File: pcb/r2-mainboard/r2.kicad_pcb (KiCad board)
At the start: 4 copper layers, 85.5 x 82.8 mm, 328 parts, among them J20 SWD+JTAG (DNP), J200 USB-C 16P, J201 Pico-Lock 504050-0391, J202 SolderPads 3x, J21 MICRO_SD(TFC-WPAPR-08), J22 HC-FPC-05-09-6RLTAG, J24 HC-FPC-05-09-8RLTAG, J26 BTH-060-01-L-D-A-K-TR, J27 BTH-060-01-L-D-A-K-TR, J28 USB-C 16P, J6 XF2M-4015-1A, Q1 AO3401A, Q2 S8050, Q6 AO3400A, Q7 AO3401A, Q8 AO3401A, Q9 AO3400A, SW20 EVQPUC02K, SW21 SW, SW22 SW, U20 STM32G0B1RCT6, U200 BQ25892RTW, U201 MAX17048G+T10, U21 INA3221, U22 INA3221, U23 LGS6302B5, U24 LGS6302B5, U26 LGS5145, U27 INA3221, U3 USBLC6-2SC6, U300 TPS7A0233DBVR, U301 TPS61022RWUR, U302 TPS63802DLAR, U303 TPS62A02DRLR, U304 TPS62A02DRLR, U31 LM321, U41 XC6SLX-FTG256, U52 MT41K64M16TW, U53 LM3630A, U54 TPS22914BYFPR, U56 TPS2553DBVR, U57 USBLC6-2SC6, U6 MT9700, U7 TPS22914BYFPR, U8 TPS22914BYFPR, U9 LGS5145, U902 W25Q128JVSIQ, X1 33.33MHz, X2 PCM-071, Y20 32.768kHz

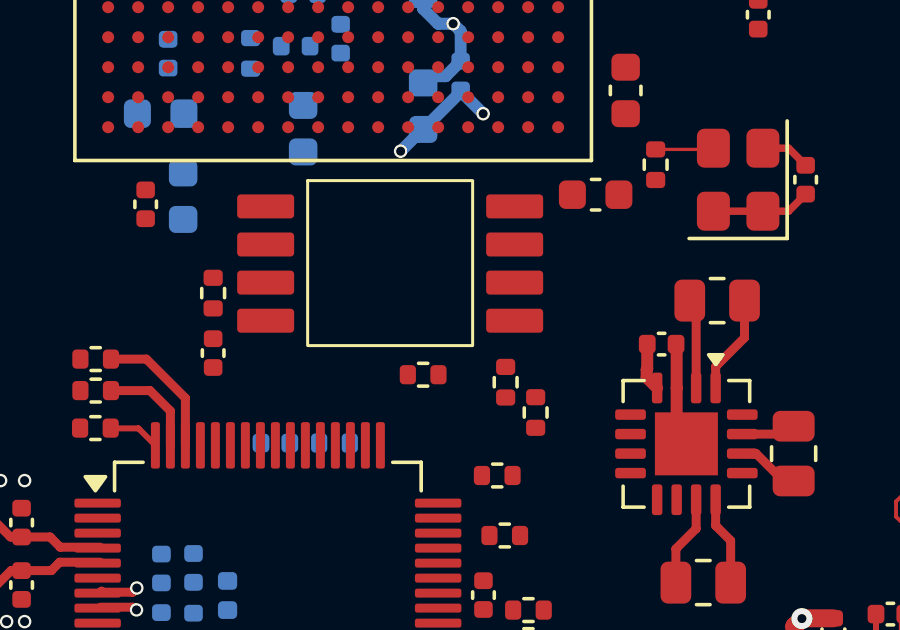
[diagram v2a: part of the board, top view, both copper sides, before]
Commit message: Declare the owner's Reflow symbol library; drop the dead library.pretty
U902 (the config NOR, was U42) uses lib_id "Reflow:WSON_Flash", but
sym-lib-table declared only "symbols" and "r2", so KiCad would report it
as a missing symbol and offer to rescue it. Declared:

  Reflow -> ${KIPRJMOD}/library/Reflow.kicad_sym

fp-lib-table also carried an entry for ${KIPRJMOD}/library.pretty, which
does not exist on disk -- an error on every project open. The real
footprint library is library/Reflow.pretty and was already declared
separately as "Reflow", so the dead entry is removed.

Verified: the netlist exports with no warnings and U902's eight nodes are
identical to what U42 had -- pin 1 NOR_CS#, 2 FPGA_MOSI, 3 NOR_IO2,
4 GND, 5 FPGA_MISO, 6 FPGA_SCLK, 7 NOR_IO3, 8 +3V3.

Not changed: tutorial_lib.kicad_sym (4 symbols) is still undeclared, and
r2.pretty is untouched -- its 8 footprints all remain in use.

Co-Authored-By: Claude Opus 5 <noreply@anthropic.com>
Claude-Session: https://claude.ai/code/session_01MHTAe6ZnhogTEgtyPcLhwG
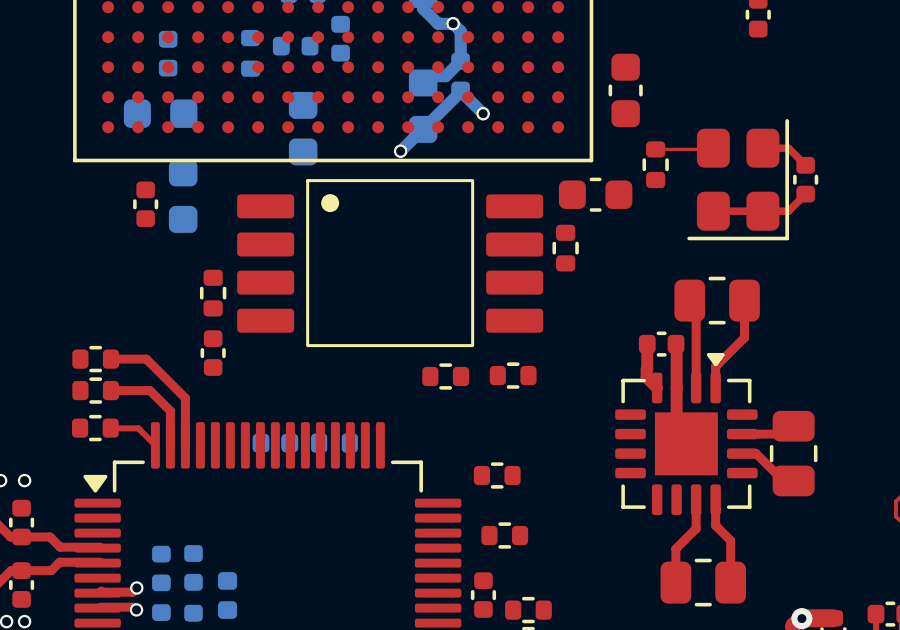
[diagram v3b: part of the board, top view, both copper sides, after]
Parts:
- moved R413 11.8 mm to (221.2, 91.2), turned to -90 degrees
- moved R412 7.51 mm to (209.5, 92.8), turned to 90 degrees
- moved R411 3.23 mm to (217.2, 95.5), turned to 180 degrees
- moved R410 0.33 mm to (219.5, 95.5), turned to 180 degrees
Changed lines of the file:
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@@
 	(footprint "Resistor_SMD:R_0402_1005Metric"
 		(layer "F.Cu")
-		(at 219.25 95.72 90)
+		(at 219.5 95.5 180)
 		(descr "Resistor SMD 0402 (1005 Metric), square (rectangular) end terminal, IPC-7351 nominal, (Body size source: IPC-SM-782 page 72, https://www.pcb-3d.com/wordpress/wp-content/uploads/ipc-sm-782a_amendment_1_and_2.pdf)")
 		(tags "resistor")
 		(property "Reference" "R410"
-			(at 0 -1.17 90)
+			(at 0 -1.17 0)
 			(layer "F.SilkS")
 			(hide yes)
@@
 		)
 		(property "Value" "10k"
-			(at 0 1.17 90)
+			(at 0 1.17 0)
 			(layer "F.Fab")
 			(effects
@@
 		)
 		(property "Datasheet" ""
-			(at 0 0 90)
+			(at 0 0 0)
 			(layer "F.Fab")
 			(hide yes)
@@
 		)
 		(property "Description" "NOR_CS# pull-up -- holds the flash deselected when neither the FPGA nor the SoM drives it"
-			(at 0 0 90)
+			(at 0 0 0)
 			(layer "F.Fab")
 			(hide yes)
@@
 		)
 		(property "KiLib_Generator" "SMD_2terminal_chip_molded"
-			(at 0 0 90)
+			(at 0 0 0)
 			(layer "F.SilkS")
 			(hide yes)
@@
 		(duplicate_pad_numbers_are_jumpers no)
 		(fp_line
-			(start -0.153641 -0.38)
-			(end 0.153641 -0.38)
+			(start -0.153641 0.38)
+			(end 0.153641 0.38)
 			(stroke
 				(width 0.12)
@@
 		)
 		(fp_line
-			(start -0.153641 0.38)
-			(end 0.153641 0.38)
+			(start -0.153641 -0.38)
+			(end 0.153641 -0.38)
 			(stroke
 				(width 0.12)
@@
 		)
 		(fp_text user "${REFERENCE}"
-			(at 0 0 90)
+			(at 0 0 180)
 			(unlocked yes)
 			(layer "F.Fab")
@@
 		)
 		(pad "1" smd roundrect
-			(at -0.51 0 90)
+			(at -0.51 0 180)
 			(size 0.54 0.64)
 			(layers "F.Cu" "F.Mask" "F.Paste")
@@
 		)
 		(pad "2" smd roundrect
-			(at 0.51 0 90)
+			(at 0.51 0 180)
 			(size 0.54 0.64)
 			(layers "F.Cu" "F.Mask" "F.Paste")
@@
 		(sheetname "/fpga_config/")
 		(sheetfile "fpga_config.kicad_sch")
-		(units
-			(unit
-				(name "A")
-				(pins "5" "2" "3" "7" "6" "1" "8" "4")
-			)
-		)
 		(attr smd)
 		(duplicate_pad_numbers_are_jumpers no)
@@
 			(layer "F.SilkS")
 		)
+		(fp_circle
+			(center -2 -2)
+			(end -2 -2.25)
+			(stroke
+				(width 0.1)
+				(type solid)
+			)
+			(fill yes)
+			(layer "F.SilkS")
+		)
 		(pad "1" smd roundrect
 			(at -4.15 -1.89)
@@
 		)
 		(pad "5" smd roundrect
-			(at 4.15 -1.89)
+			(at 4.15 1.92)
 			(size 1.9 0.8)
 			(layers "F.Cu" "F.Mask" "F.Paste")
@@
 		)
 		(pad "6" smd roundrect
-			(at 4.15 -0.62)
+			(at 4.15 0.65)
 			(size 1.9 0.8)
 			(layers "F.Cu" "F.Mask" "F.Paste")
@@
 		)
 		(pad "7" smd roundrect
-			(at 4.15 0.65)
+			(at 4.15 -0.62)
 			(size 1.9 0.8)
 			(layers "F.Cu" "F.Mask" "F.Paste")
@@
 		)
 		(pad "8" smd roundrect
-			(at 4.15 1.92)
+			(at 4.15 -1.89)
 			(size 1.9 0.8)
 			(layers "F.Cu" "F.Mask" "F.Paste")
@@
 	(footprint "Resistor_SMD:R_0402_1005Metric"
 		(layer "F.Cu")
-		(at 216.5 95.47)
+		(at 209.5 92.75 90)
 		(descr "Resistor SMD 0402 (1005 Metric), square (rectangular) end terminal, IPC-7351 nominal, (Body size source: IPC-SM-782 page 72, https://www.pcb-3d.com/wordpress/wp-content/uploads/ipc-sm-782a_amendment_1_and_2.pdf)")
 		(tags "resistor")
 		(property "Reference" "R412"
-			(at 0 -1.17 0)
+			(at 0 -1.17 90)
 			(layer "F.SilkS")
 			(hide yes)
@@
 		)
 		(property "Value" "10k"
-			(at 0 1.17 0)
+			(at 0 1.17 90)
 			(layer "F.Fab")
 			(effects
@@
 		)
 		(property "Datasheet" ""
-			(at 0 0 0)
+			(at 0 0 90)
 			(layer "F.Fab")
 			(hide yes)
@@
 		)
 		(property "Description" "UG380 Fig 2-13 note 4: MISO[2]/MISO[3] need pull-ups to VCCO_2."
-			(at 0 0 0)
+			(at 0 0 90)
 			(layer "F.Fab")
 			(hide yes)
@@
 		)
 		(property "KiLib_Generator" "SMD_2terminal_chip_molded"
-			(at 0 0 0)
+			(at 0 0 90)
 			(layer "F.SilkS")
 			(hide yes)
@@
 		)
 		(fp_text user "${REFERENCE}"
-			(at 0 0 0)
+			(at 0 0 90)
 			(unlocked yes)
 			(layer "F.Fab")
@@
 		)
 		(pad "1" smd roundrect
-			(at -0.51 0)
+			(at -0.51 0 90)
 			(size 0.54 0.64)
 			(layers "F.Cu" "F.Mask" "F.Paste")
@@
 		)
 		(pad "2" smd roundrect
-			(at 0.51 0)
+			(at 0.51 0 90)
 			(size 0.54 0.64)
 			(layers "F.Cu" "F.Mask" "F.Paste")
@@
 	(footprint "Resistor_SMD:R_0402_1005Metric"
 		(layer "F.Cu")
-		(at 209.5 92.75 90)
+		(at 221.25 91.25 -90)
 		(descr "Resistor SMD 0402 (1005 Metric), square (rectangular) end terminal, IPC-7351 nominal, (Body size source: IPC-SM-782 page 72, https://www.pcb-3d.com/wordpress/wp-content/uploads/ipc-sm-782a_amendment_1_and_2.pdf)")
 		(tags "resistor")
@@
 		(duplicate_pad_numbers_are_jumpers no)
 		(fp_line
-			(start -0.153641 -0.38)
-			(end 0.153641 -0.38)
+			(start -0.153641 0.38)
+			(end 0.153641 0.38)
 			(stroke
 				(width 0.12)
@@
 		)
 		(fp_line
-			(start -0.153641 0.38)
-			(end 0.153641 0.38)
+			(start -0.153641 -0.38)
+			(end 0.153641 -0.38)
 			(stroke
 				(width 0.12)
@@
 		)
 		(fp_text user "${REFERENCE}"
-			(at 0 0 90)
+			(at 0 0 270)
 			(unlocked yes)
 			(layer "F.Fab")
@@
 		)
 		(pad "1" smd roundrect
-			(at -0.51 0 90)
+			(at -0.51 0 270)
 			(size 0.54 0.64)
 			(layers "F.Cu" "F.Mask" "F.Paste")
@@
 		)
 		(pad "2" smd roundrect
-			(at 0.51 0 90)
+			(at 0.51 0 270)
 			(size 0.54 0.64)
 			(layers "F.Cu" "F.Mask" "F.Paste")
@@
 	(footprint "Resistor_SMD:R_0402_1005Metric"
 		(layer "F.Cu")
-		(at 220.25 96.73 90)
+		(at 217.25 95.53 180)
 		(descr "Resistor SMD 0402 (1005 Metric), square (rectangular) end terminal, IPC-7351 nominal, (Body size source: IPC-SM-782 page 72, https://www.pcb-3d.com/wordpress/wp-content/uploads/ipc-sm-782a_amendment_1_and_2.pdf)")
 		(tags "resistor")
 		(property "Reference" "R411"
-			(at 0 -1.17 90)
+			(at 0 -1.17 0)
 			(layer "F.SilkS")
 			(hide yes)
@@
 		)
 		(property "Value" "100R"
-			(at 0 1.17 90)
+			(at 0 1.17 0)
 			(layer "F.Fab")
 			(effects
@@
 		)
 		(property "Datasheet" ""
-			(at 0 0 90)
+			(at 0 0 0)
 			(layer "F.Fab")
 			(hide yes)
@@
 		)
 		(property "Description" "Series limit on the SoM's NOR chip select: the FPGA drives CSO_B during configuration, so the two briefly contend if software gets it wrong"
-			(at 0 0 90)
+			(at 0 0 0)
 			(layer "F.Fab")
 			(hide yes)
@@
 		)
 		(property "KiLib_Generator" "SMD_2terminal_chip_molded"
-			(at 0 0 90)
+			(at 0 0 0)
 			(layer "F.SilkS")
 			(hide yes)
@@
 		(duplicate_pad_numbers_are_jumpers no)
 		(fp_line
-			(start -0.153641 -0.38)
-			(end 0.153641 -0.38)
+			(start -0.153641 0.38)
+			(end 0.153641 0.38)
 			(stroke
 				(width 0.12)
@@
 		)
 		(fp_line
-			(start -0.153641 0.38)
-			(end 0.153641 0.38)
+			(start -0.153641 -0.38)
+			(end 0.153641 -0.38)
 			(stroke
 				(width 0.12)
@@
 		)
 		(fp_text user "${REFERENCE}"
-			(at 0 0 90)
+			(at 0 0 180)
 			(unlocked yes)
 			(layer "F.Fab")
@@
 		)
 		(pad "1" smd roundrect
-			(at -0.51 0 90)
+			(at -0.51 0 180)
 			(size 0.54 0.64)
 			(layers "F.Cu" "F.Mask" "F.Paste")
@@
 		)
 		(pad "2" smd roundrect
-			(at 0.51 0 90)
+			(at 0.51 0 180)
 			(size 0.54 0.64)
 			(layers "F.Cu" "F.Mask" "F.Paste")

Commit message: Recover from the KiCad crash; finish the USB1_D+/D- rename
KiCad crashed and deleted 150 tracked files plus 19 untracked ones.
Recovery, in the order that matters:

  1. copied _restore_backup_2026-08-31T20-57-08-688 aside (261 MB)
  2. rescued the 4 untracked files that existed only there -- the
     PHYTEC PCM-071 STEP/x_t/Basic models and the library/3dmodels copy.
     The other 15 were __pycache__, .lck and .bak.
  3. git checkout of the 150 deletions (deletions only, so the six
     modified files were never touched)
  4. three files the crash had *rolled back* rather than deleted, and
     which git checkout therefore missed, restored from HEAD:
       r2.kicad_sym    -- was 11 symbols, missing TPS2553DBV,
                          BTH-060_AB/CD and BOM_ITEM, and carrying the
                          superseded PCM-071 symbol: the pre-2026-08-20
                          state, before the SoM was split in two
       sym-lib-table   -- had lost the Reflow declaration
       fp-lib-table    -- had lost Reflow and (version 7)

r2.kicad_pcb was not damaged -- 328 footprints, 471 segments, same as
HEAD. Rescuing PCM-071_1573-1.STEP also repairs X2's 3D model path,
which an earlier restore had broken.

Separately, the USB1 net rename is finished at the owner's request:
som.kicad_sch USB1_DM/DP -> USB1_D-/D+ (the J26 X_USB1_* pin names are
PHYTEC's and are untouched), and a USB1_+ typo on U57's second ESD stub
in io_expansion corrected to USB1_D+. sheet_pins + wire_root re-run:
113 names on 233 sheet pins, 113 joined, 0 one-sided. All five USB1
nets verified node-for-node.

⚠ The tree is mid-renumber (J200/U200/U300... appearing) and carries one
severed net: +3V3_TOUCH reaches only J22.1, while U54.A1 and C517.1 sit
on an unnamed Net-(U54-OUT). Committed as-is so the recovery is not at
risk from another crash; the break is called out rather than hidden.

Co-Authored-By: Claude Opus 5 <noreply@anthropic.com>
Claude-Session: https://claude.ai/code/session_01MHTAe6Znh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
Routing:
- net GND: vias 25 -> 22
- net +3V3: vias 7 -> 10
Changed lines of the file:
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@@
 		)
 		(embedded_fonts no)
-		(model "${KIPRJMOD}/3dmodels/BTH-060-01-L-D-A-K-TR.stp"
+		(model "${KIPRJMOD}/library/3dmodels/BTH-060-01-L-D-A-K-TR.stp"
 			(offset
 				(xyz 0 0 0)
@@
 		)
 		(embedded_fonts no)
-		(model "${KIPRJMOD}/3dmodels/HRO_TYPE-C-31-M-12.step"
+		(model "${KIPRJMOD}/library/3dmodels/HRO_TYPE-C-31-M-12.step"
 			(offset
 				(xyz -4.47 -3.6 0)
@@
 		)
 		(embedded_fonts no)
-		(model "${KIPRJMOD}/datasheets/SoM Phycore AM62x/PCM-071_1573-1_3d/PCM-071_1573-1.STEP"
+		(model "${KIPRJMOD}/library/3dmodels/PCM-071_1573-1.STEP"
 			(offset
 				(xyz -16 -21.5 3.212)
@@
 		)
 		(embedded_fonts no)
-		(model "${KIPRJMOD}/3dmodels/MOLEX 5040500391/5040500391.stp"
+		(model "${KIPRJMOD}/library/3dmodels/MOLEX 5040500391/5040500391.stp"
 			(offset
 				(xyz 1.5 -5.35 0)
@@
 		)
 		(embedded_fonts no)
+		(model "${KICAD10_3DMODEL_DIR}/Package_SO.3dshapes/SOIC-8_5.3x5.3mm_P1.27mm.step"
+			(offset
+				(xyz 0 0 0)
+			)
+			(scale
+				(xyz 1 1 1)
+			)
+			(rotate
+				(xyz 0 0 0)
+			)
+		)
 	)
 	(footprint "Resistor_SMD:R_0402_1005Metric"
@@
 		)
 		(embedded_fonts no)
-		(model "${KIPRJMOD}/3dmodels/HRO_TYPE-C-31-M-12.step"
+		(model "${KIPRJMOD}/library/3dmodels/HRO_TYPE-C-31-M-12.step"
 			(offset
 				(xyz -4.47 -3.6 0)
@@
 		)
 		(embedded_fonts no)
-		(model "${KIPRJMOD}/3dmodels/BTH-060-01-L-D-A-K-TR.stp"
+		(model "${KIPRJMOD}/library/3dmodels/BTH-060-01-L-D-A-K-TR.stp"
 			(offset
 				(xyz 0 0 0)
@@
 		)
 		(embedded_fonts no)
-		(model "${KIPRJMOD}/3dmodels/HY-TF1007B.STEP"
+		(model "${KIPRJMOD}/library/3dmodels/HY-TF1007B.STEP"
 			(offset
 				(xyz -7.2 -7.4 0)
@@
 	)
 	(via
+		(at 199.765 100.8)
+		(size 0.45)
+		(drill 0.3)
+		(layers "F.Cu" "B.Cu")
+		(net "GND")
+	)
+	(via
 		(at 200.515 99)
 		(size 0.45)
@@
 	)
 	(via
-		(at 200.665 103.8)
-		(size 0.45)
-		(drill 0.3)
-		(layers "F.Cu" "B.Cu")
-		(net "GND")
-	)
-	(via
 		(at 191.55 70.7125)
 		(size 0.45)
@@
 	)
 	(via
-		(at 203.215 99)
-		(size 0.45)
-		(drill 0.3)
-		(layers "F.Cu" "B.Cu")
-		(net "GND")
-	)
-	(via
-		(at 199.665 102.95)
-		(size 0.45)
-		(drill 0.3)
-		(layers "F.Cu" "B.Cu")
-		(net "GND")
-	)
-	(via
-		(at 202.415 99)
-		(size 0.45)
-		(drill 0.3)
-		(layers "F.Cu" "B.Cu")
-		(net "GND")
-	)
-	(via
 		(at 199.715 101.95)
 		(size 0.45)
@@
 	)
 	(via
+		(at 203.215 103.7)
+		(size 0.45)
+		(drill 0.3)
+		(layers "F.Cu" "B.Cu")
+		(net "GND")
+	)
+	(via
 		(at 239.7 45.825)
 		(size 0.8)
@@
 	)
 	(via
-		(at 202.615 103.7)
-		(size 0.45)
-		(drill 0.3)
-		(layers "F.Cu" "B.Cu")
-		(net "GND")
-	)
-	(via
 		(at 201.815 99)
 		(size 0.45)
@@
 	)
 	(via
-		(at 199.765 100.8)
+		(at 201.965 103.75)
 		(size 0.45)
 		(drill 0.3)
@@
 	)
 	(via
-		(at 201.965 103.75)
+		(at 200.665 103.8)
 		(size 0.45)
 		(drill 0.3)
@@
 	)
 	(via
+		(at 203.215 99)
+		(size 0.45)
+		(drill 0.3)
+		(layers "F.Cu" "B.Cu")
+		(net "+3V3")
+	)
+	(via
 		(at 201.165 99)
 		(size 0.45)
@@
 	)
 	(via
-		(at 203.215 103.7)
+		(at 199.665 102.95)
+		(size 0.45)
+		(drill 0.3)
+		(layers "F.Cu" "B.Cu")
+		(net "+3V3")
+	)
+	(via
+		(at 202.415 99)
+		(size 0.45)
+		(drill 0.3)
+		(layers "F.Cu" "B.Cu")
+		(net "+3V3")
+	)
+	(via
+		(at 202.615 103.7)
 		(size 0.45)
 		(drill 0.3)
